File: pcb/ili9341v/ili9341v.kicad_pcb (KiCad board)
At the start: 2 copper layers, 36.4 x 11 mm, 6 parts, among them J2 Conn_01x14_Socket

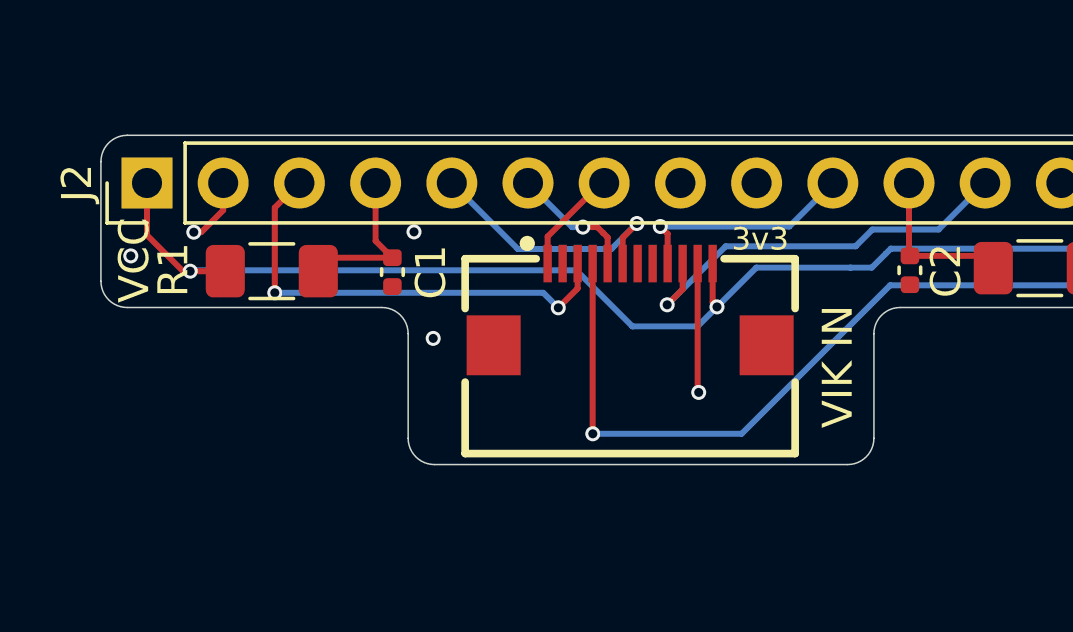
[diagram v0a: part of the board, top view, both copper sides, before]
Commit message: added MISO for SD card support, added jumper to select between backlight and sd card, defaults to backlight
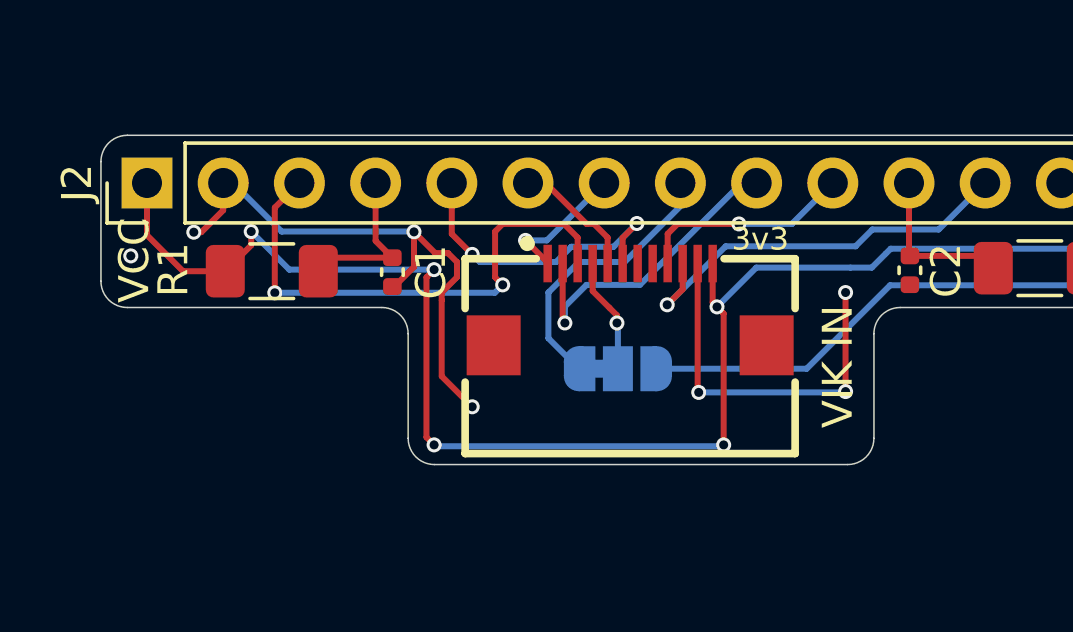
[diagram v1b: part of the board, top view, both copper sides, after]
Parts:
- added JP1: SolderJumper_3_Bridged12, Jumper:SolderJumper-3_P1.3mm_Bridged12_RoundedPad1.0x1.5mm_NumberLabels, B.Cu at (173.8, 106.7)
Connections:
- J2 pad 14: GPIO_AD2 -> Net-(J2-Pin_14)
- J2 pad 8: unconnected-(J2-Pin_8-Pad8) -> Net-(J2-Pin_8)
- J2 pad 9: unconnected-(J2-Pin_9-Pad9) -> MISO
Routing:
- net GPIO_AD2: track 30.8 -> 3.85 mm, vias 2 -> 1
- net GND: track 6.50 -> 31.2 mm, vias 5 -> 7
- net Net-(J2-Pin_14): track 0.00 -> 22.1 mm, vias 0 -> 1
- net MISO: track 0.00 -> 10.7 mm, vias 0 -> 1
- net +3V3: track 41.4 -> 51.5 mm, vias 3 -> 6
- net Net-(J2-Pin_8): track 0.00 -> 9.33 mm
- net SPI_CS: track 15.4 -> 17.5 mm
- net GPIO_AD1: track 8.97 -> 10.3 mm, vias 1 -> 2
- net SCLK: track 3.53 -> 4.49 mm, vias 0 -> 1
- net MOSI: track 4.28 -> 4.27 mm, vias 1 -> 0
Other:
- board text added: "SDCard-3 BL-1"

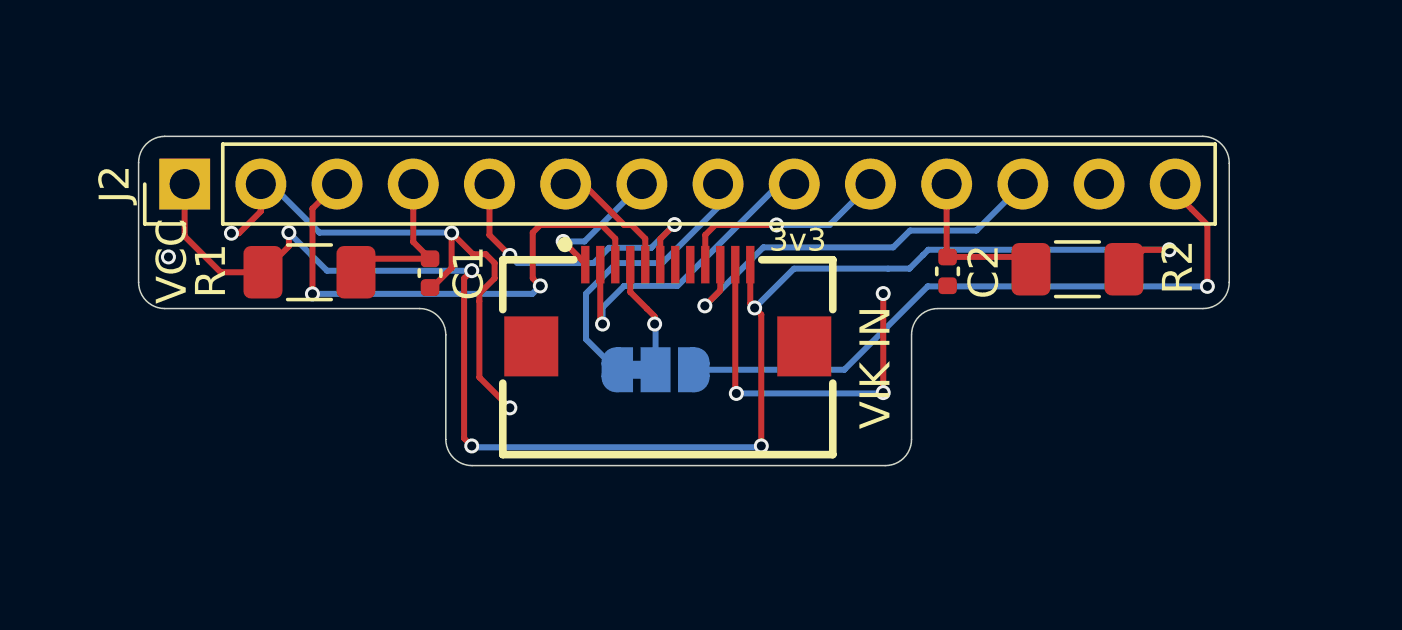
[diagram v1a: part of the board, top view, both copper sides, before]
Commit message: ili9341v display module - updated to use hand solderable capacitors, 1206 instead of 0402
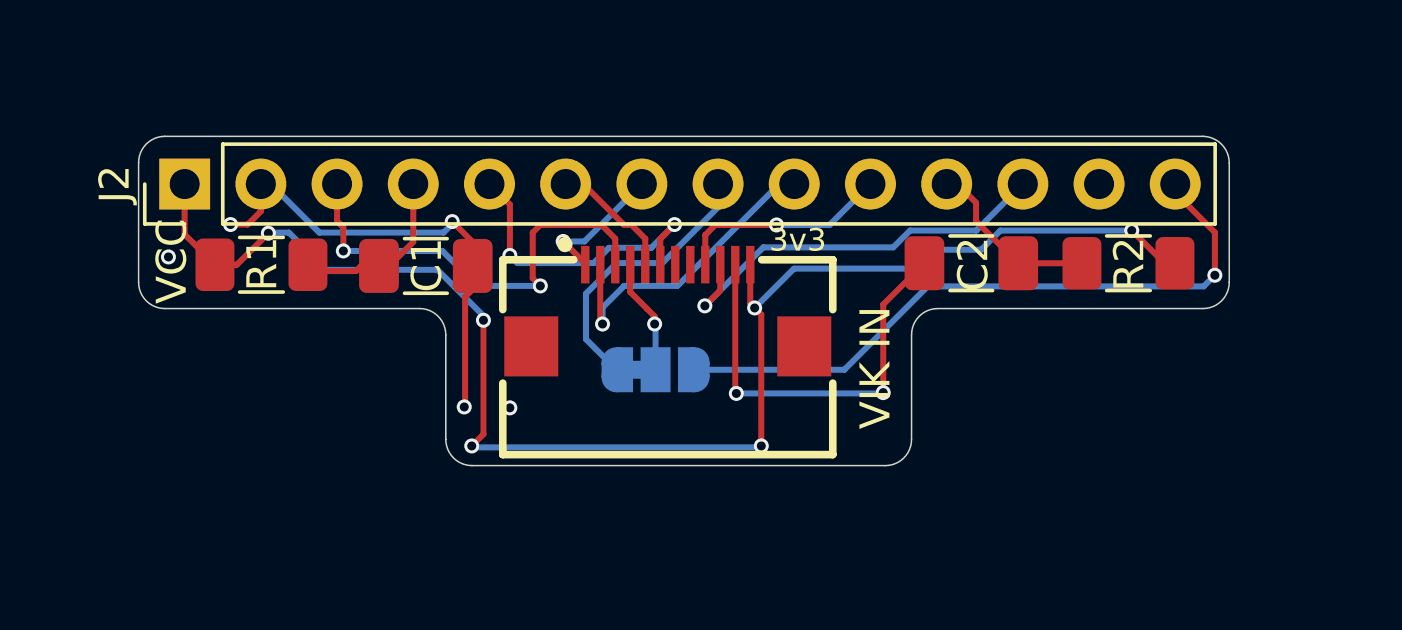
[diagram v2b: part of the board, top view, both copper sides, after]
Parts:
- C1, C2: footprint Capacitor_SMD:C_0402_1005Metric -> Capacitor_SMD:C_1206_3216Metric_Pad1.33x1.80mm_HandSolder
- moved R2 1.71 mm to (189.5, 103.1)
- moved R1 1.62 mm to (160.6, 103.2)
- moved C2 0.84 mm to (184.3, 103.1), turned to 0 degrees
- moved C1 0.28 mm to (166.1, 103.2), turned to 180 degrees
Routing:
- net SPI_CS: track 17.5 -> 15.2 mm
- net +3V3: track 51.5 -> 49.6 mm
- net GND: track 31.2 -> 30.0 mm
- net Net-(J2-Pin_11): track 5.39 -> 5.96 mm
- net Net-(J2-Pin_4): track 5.38 -> 5.93 mm
